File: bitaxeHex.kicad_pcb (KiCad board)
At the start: 4 copper layers, 84.5 x 129.5 mm, 371 parts, among them J1 Conn_01x01, J2 Conn_01x01, J3 Conn_02x05_Odd_Even, J4 TC2030-IDC, J5 Conn_01x04, J6 Conn_01x06, J7 USB_C_Receptacle_USB2.0, J8 Conn_01x04, J9 Conn_01x04, SW1 SWITCH-SPST, SW2 SWITCH-SPST, U1 LMR54410, U10 AP7331, U11 AP7331, U12 BM1368_mode1, U13 BM1368_mode0, U14 25MHz, U15 TLV3544, U16 AP7331, U17 AP7331, U18 BM1368_mode0, U19 25MHz, U2 RT9080-33GJ5, U21 TLV3544, U23 AP7331, U24 AP7331, U25 BM1368_mode1, U26 25MHz, U27 BM1368_mode1, U28 BM1368_mode1, U3 TPS546D24ARVFR, U4 MIC5504-MS, U5 SN74AVC4T774, U6 ESP32-S3-WROOM-1, U7 TMP1075, U8 TMP1075, U9 EMC2302, Y1 32.768kHz

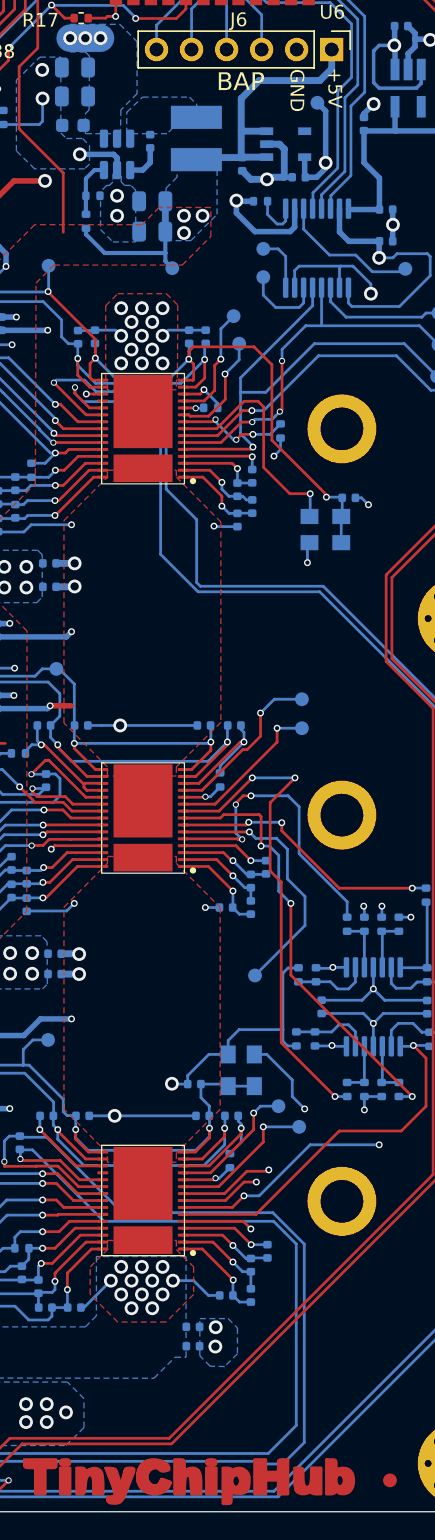
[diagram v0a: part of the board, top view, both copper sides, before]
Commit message: Add CE logo on it
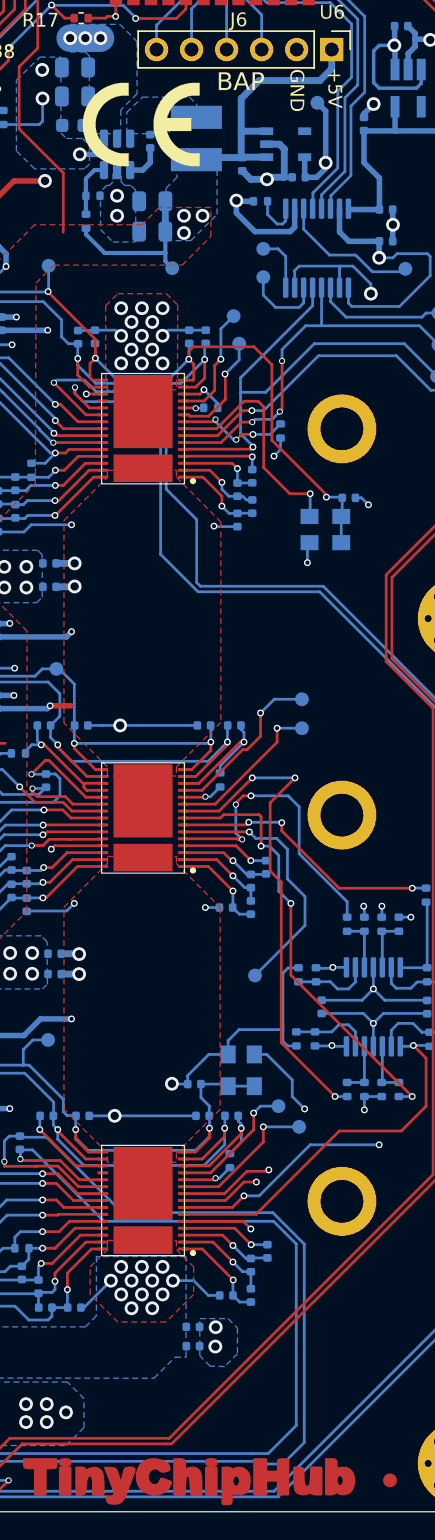
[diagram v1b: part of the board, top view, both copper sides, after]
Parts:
- added REF**: CE-Logo_8.5x6mm_SilkScreen, Symbol:CE-Logo_8.5x6mm_SilkScreen, F.Cu at (108.0, 74.9)
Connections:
- C47 pad 1: Net-(U28-VDDIO_08_0) -> /BM1368-1/0V8
- C53 pad 1: GND -> /BM1368-1/0V8
- C58 pad 1: GND -> /BM1368-1/0V8
- C67 pad 1: GND -> /BM1368-1/0V8
- C76 pad 1: GND -> /BM1368-1/0V8
- R31 pad 2: GND -> /BM1368-1/0V8
- TP35 pad 1: GND -> /BM1368-1/0V8
- U10 pad 5: GND -> /BM1368-1/0V8
- U12 pad 14: GND -> /BM1368-1/0V8
- U12 pad 17: GND -> /BM1368-1/0V8
- U28 pad 14: Net-(U28-VDDIO_08_0) -> /BM1368-1/0V8
- U28 pad 17: GND -> /BM1368-1/0V8
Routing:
- net /BM1368-1/0V8: track 0.00 -> 69.4 mm, vias 0 -> 4
- net GND: track 446.5 -> 377.1 mm, vias 114 -> 110

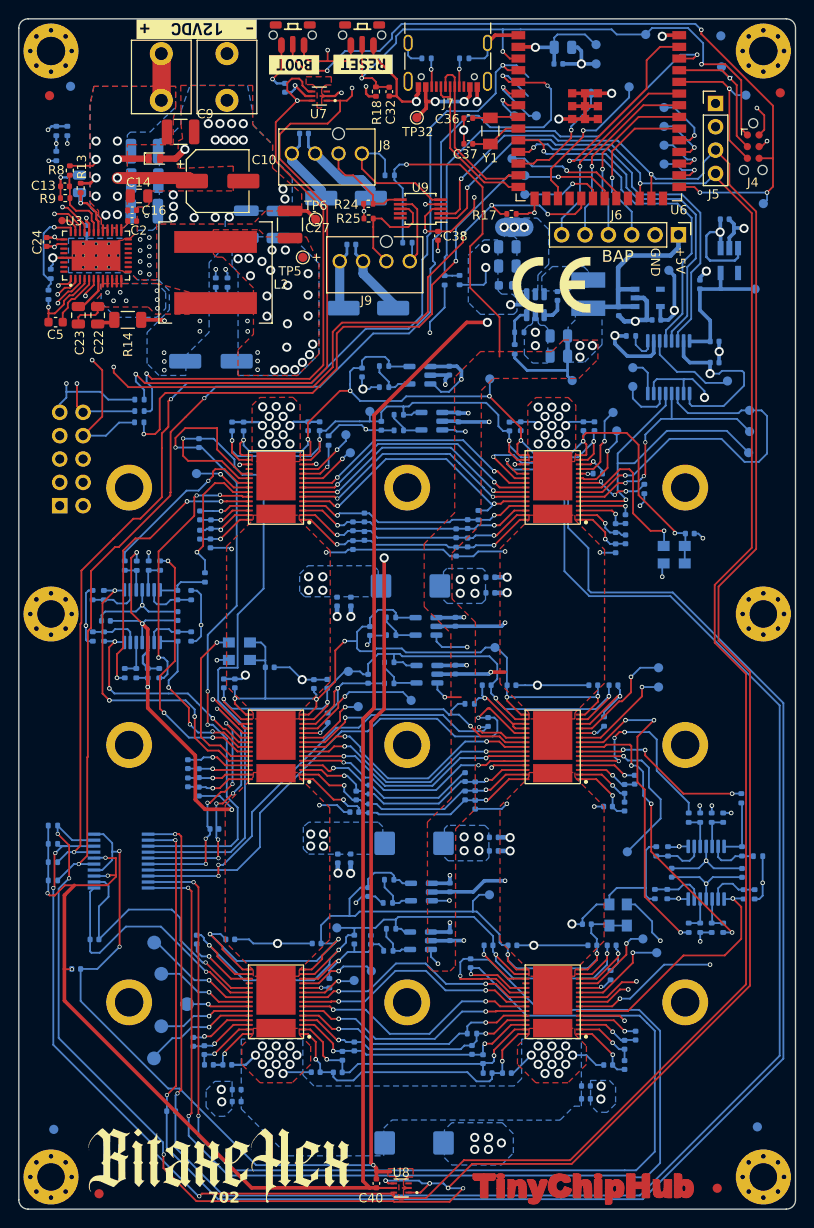
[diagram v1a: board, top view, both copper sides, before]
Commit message: Add resisters for MAX6689
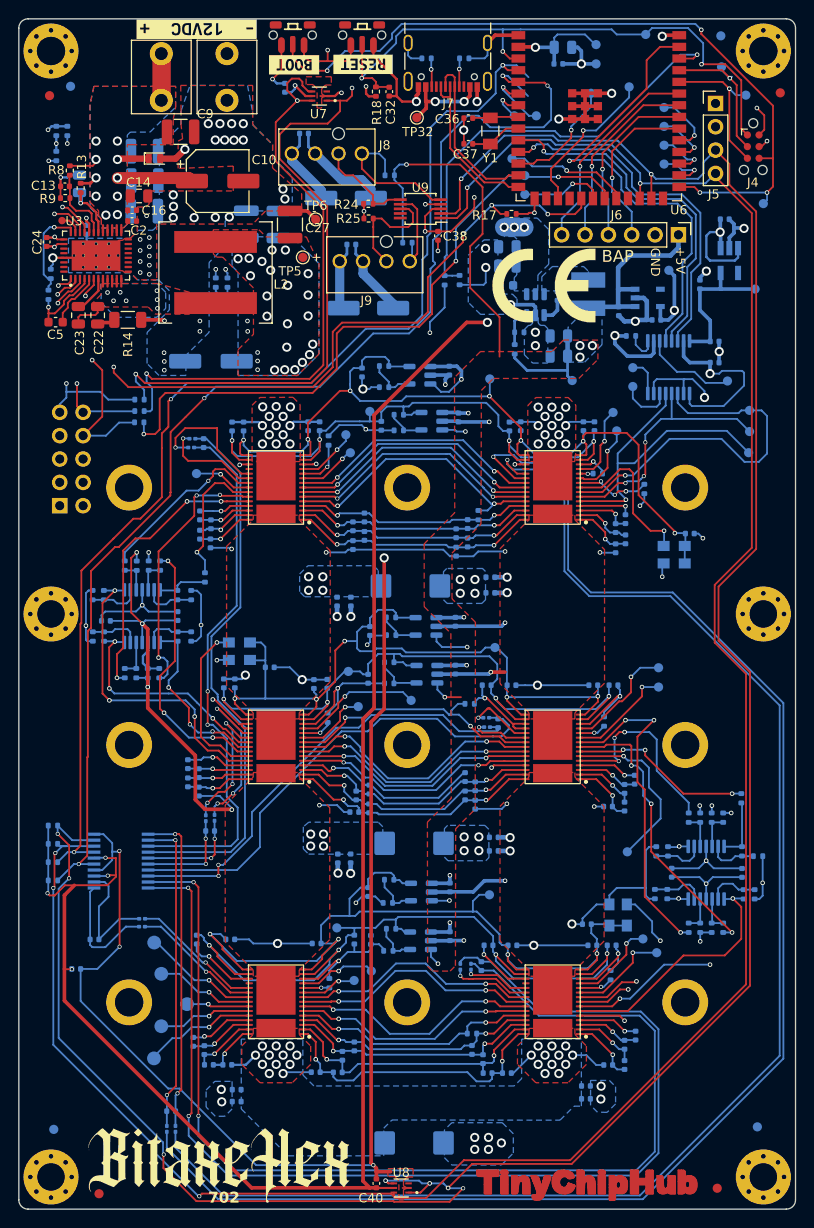
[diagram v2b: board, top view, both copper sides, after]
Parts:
- removed the REF** at (108.0, 74.9)
- added R88: 100R, Resistor_SMD:R_0201_0603Metric, B.Cu at (63.4, 144.8)
- added R89: 100R, Resistor_SMD:R_0201_0603Metric, B.Cu at (63.4, 143.9)
- added R90: 100R, Resistor_SMD:R_0201_0603Metric, B.Cu at (98.0, 149.1)
- added R91: 100R, Resistor_SMD:R_0201_0603Metric, B.Cu at (99.2, 149.1)
- added R92: 100R, Resistor_SMD:R_0201_0603Metric, B.Cu at (100.9, 123.1)
- added R93: 100R, Resistor_SMD:R_0201_0603Metric, B.Cu at (100.8, 122.0)
- added R94: 100R, Resistor_SMD:R_0201_0603Metric, B.Cu at (70.3, 133.0)
- added R95: 100R, Resistor_SMD:R_0201_0603Metric, B.Cu at (71.3, 132.9)
- added R96: 100R, Resistor_SMD:R_0201_0603Metric, B.Cu at (68.9, 91.7)
- added R97: 100R, Resistor_SMD:R_0201_0603Metric, B.Cu at (68.8, 92.6)
- added R98: 100R, Resistor_SMD:R_0201_0603Metric, B.Cu at (66.1, 166.8)
- added R99: 100R, Resistor_SMD:R_0201_0603Metric, B.Cu at (67.0, 166.8)
- added REF**: CE-Logo_11.2x8mm_SilkScreen, Symbol:CE-Logo_11.2x8mm_SilkScreen, F.Cu at (107.1, 75.0)
- C40: value 0.1uF -> 311-3342-1-ND
- moved C156 1.21 mm to (100.3, 149.1)
- moved C155 1.10 mm to (102.1, 122.6)
- moved REF** 0.60 mm to (111.2, 173.5)
- moved REF** 0.57 mm to (111.2, 173.0)
- moved C154 0.52 mm to (70.8, 134.4)
- moved C153 0.50 mm to (70.1, 92.2)
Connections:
- C152 pad 1: /BM1368-1/TEMP_P1 -> Net-(U20-DXP1)
- C152 pad 2: /BM1368-1/TEMP_N1 -> Net-(U20-DXN1)
- C153 pad 1: /BM1368-1/TEMP_P2 -> Net-(U20-DXP2)
- C153 pad 2: /BM1368-1/TEMP_N2 -> Net-(U20-DXN2)
- C154 pad 1: /BM1368-2/TEMP_P3 -> Net-(U20-DXP3)
- C154 pad 2: /BM1368-2/TEMP_N3 -> Net-(U20-DXN3)
- C155 pad 1: /BM1368-2/TEMP_P4 -> Net-(U20-DXP4)
- C155 pad 2: /BM1368-2/TEMP_N4 -> Net-(U20-DXN4)
- C156 pad 1: /BM1368-3/TEMP_P5 -> Net-(U20-DXP5)
- C156 pad 2: /BM1368-3/TEMP_N5 -> Net-(U20-DXN5)
- C157 pad 1: /BM1368-3/TEMP_P6 -> Net-(U20-DXP6)
- C157 pad 2: /BM1368-3/TEMP_N6 -> Net-(U20-DXN6)
- C47 pad 1: /BM1368-1/0V8 -> Net-(U28-VDDIO_08_0)
- C53 pad 1: /BM1368-1/0V8 -> GND
- C58 pad 1: /BM1368-1/0V8 -> GND
- C67 pad 1: /BM1368-1/0V8 -> GND
- C76 pad 1: /BM1368-1/0V8 -> GND
- R31 pad 2: /BM1368-1/0V8 -> GND
- TP35 pad 1: /BM1368-1/0V8 -> GND
- U10 pad 5: /BM1368-1/0V8 -> GND
- U12 pad 14: /BM1368-1/0V8 -> GND
- U12 pad 17: /BM1368-1/0V8 -> GND
- U20 pad 1: /BM1368-1/TEMP_P1 -> Net-(U20-DXP1)
- U20 pad 10: /BM1368-3/TEMP_N5 -> Net-(U20-DXN5)
- U20 pad 11: /BM1368-3/TEMP_N6 -> Net-(U20-DXN6)
- U20 pad 12: /BM1368-3/TEMP_P6 -> Net-(U20-DXP6)
- U20 pad 2: /BM1368-1/TEMP_N1 -> Net-(U20-DXN1)
- U20 pad 3: /BM1368-1/TEMP_P2 -> Net-(U20-DXP2)
- U20 pad 4: /BM1368-1/TEMP_N2 -> Net-(U20-DXN2)
- U20 pad 5: /BM1368-2/TEMP_P3 -> Net-(U20-DXP3)
- U20 pad 6: /BM1368-2/TEMP_N3 -> Net-(U20-DXN3)
- U20 pad 7: /BM1368-2/TEMP_P4 -> Net-(U20-DXP4)
- U20 pad 8: /BM1368-2/TEMP_N4 -> Net-(U20-DXN4)
- U20 pad 9: /BM1368-3/TEMP_P5 -> Net-(U20-DXP5)
- U28 pad 14: /BM1368-1/0V8 -> Net-(U28-VDDIO_08_0)
- U28 pad 17: /BM1368-1/0V8 -> GND
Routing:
- net /BM1368-3/TEMP_N5: track 134.5 -> 8.57 mm, vias 3 -> 1
- net Net-(U20-DXN5): track 0.00 -> 124.2 mm, vias 0 -> 2
- net /BM1368-3/TEMP_P5: track 128.1 -> 7.08 mm, vias 3 -> 1
- net Net-(U20-DXP5): track 0.00 -> 121.0 mm, vias 0 -> 2
- net /BM1368-1/0V8: track 69.4 -> 0.00 mm, vias 4 -> 0
- net GND: track 377.1 -> 446.5 mm, vias 110 -> 114
- net /BM1368-1/TEMP_N2: track 76.0 -> 10.8 mm
- net Net-(U20-DXN2): track 0.00 -> 60.2 mm
- net /BM1368-1/TEMP_P2: track 73.1 -> 14.3 mm, vias 3 -> 1
- net Net-(U20-DXP2): track 0.00 -> 58.7 mm, vias 0 -> 2
- net Net-(U20-DXP4): track 0.00 -> 52.3 mm
- net /BM1368-2/TEMP_P4: track 58.2 -> 7.25 mm
- net Net-(U20-DXN4): track 0.00 -> 49.5 mm, vias 0 -> 2
- net /BM1368-2/TEMP_N4: track 54.2 -> 6.27 mm, vias 3 -> 1
- net /BM1368-1/TEMP_P1: track 199.9 -> 163.7 mm, vias 3 -> 1
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
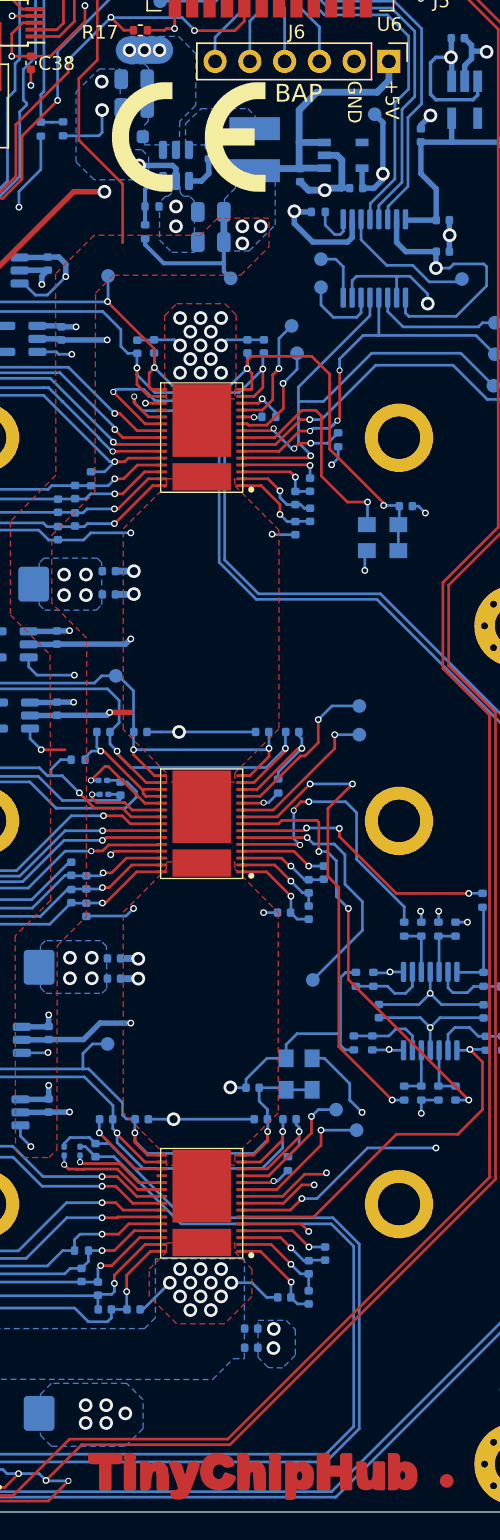
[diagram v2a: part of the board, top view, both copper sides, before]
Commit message: Reset to 1V8
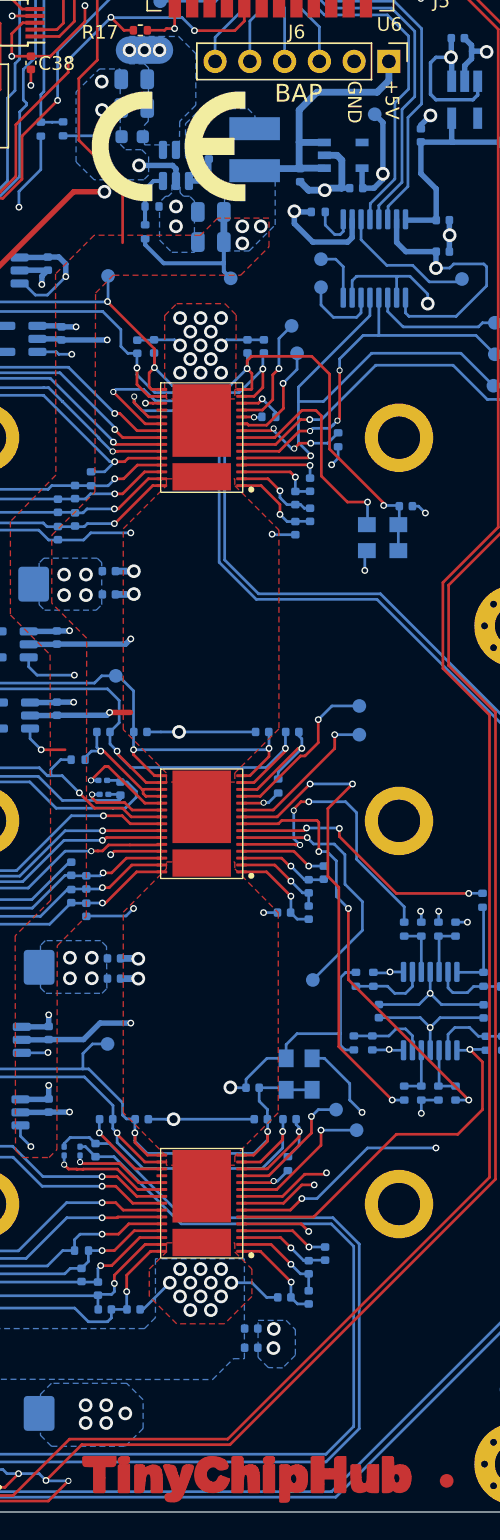
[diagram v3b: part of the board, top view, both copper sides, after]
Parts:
- R30, R38, R64: value 110k -> 115k
- R32, R40, R66: value 220k -> 402k
- moved REF** 1.62 mm to (105.7, 75.7)
- moved REF** 0.50 mm to (110.8, 173.2)
- moved REF** 0.39 mm to (110.8, 173.7)
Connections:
- net /BM1368-1/1V2 renamed /BM1368-1/1V8
- net /BM1368-2/1V2 renamed /BM1368-2/1V8
- net /BM1368-3/1V2 renamed /BM1368-3/1V8
- C25 pad 1: /Power/1V2 -> /1V8
- C34 pad 2: /1V2 -> /1V8
- C47 pad 1: Net-(U28-VDDIO_08_0) -> /BM1368-1/0V8
- C53 pad 1: GND -> /BM1368-1/0V8
- C58 pad 1: GND -> /BM1368-1/0V8
- C67 pad 1: GND -> /BM1368-1/0V8
- C76 pad 1: GND -> /BM1368-1/0V8
- R31 pad 2: GND -> /BM1368-1/0V8
- TP35 pad 1: GND -> /BM1368-1/0V8
- TP4 pad 1: /Power/1V2 -> /1V8
- U10 pad 5: GND -> /BM1368-1/0V8
- U12 pad 14: GND -> /BM1368-1/0V8
- U12 pad 17: GND -> /BM1368-1/0V8
- U28 pad 14: Net-(U28-VDDIO_08_0) -> /BM1368-1/0V8
- U28 pad 17: GND -> /BM1368-1/0V8
- U4 pad 5: /Power/1V2 -> /1V8
- U5 pad 16: /1V2 -> /1V8
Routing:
- net /BM1368-1/0V8: track 0.00 -> 69.4 mm, vias 0 -> 4
- net GND: track 446.5 -> 377.1 mm, vias 114 -> 110
- net /1V8: track 0.00 -> 16.2 mm
- net /1V2: track 16.2 -> 0.00 mm
